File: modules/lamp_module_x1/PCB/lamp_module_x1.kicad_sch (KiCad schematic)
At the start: 24 parts, among them J1 Screw_Terminal_01x02, J2 Screw_Terminal_01x03, J3 Conn_01x06_Socket, J4 Conn_01x03_Socket, K1 12V 5A, Q1 2N7002H, U1 AMS1117-3.3, U2 ESP-12E, U4 PC817

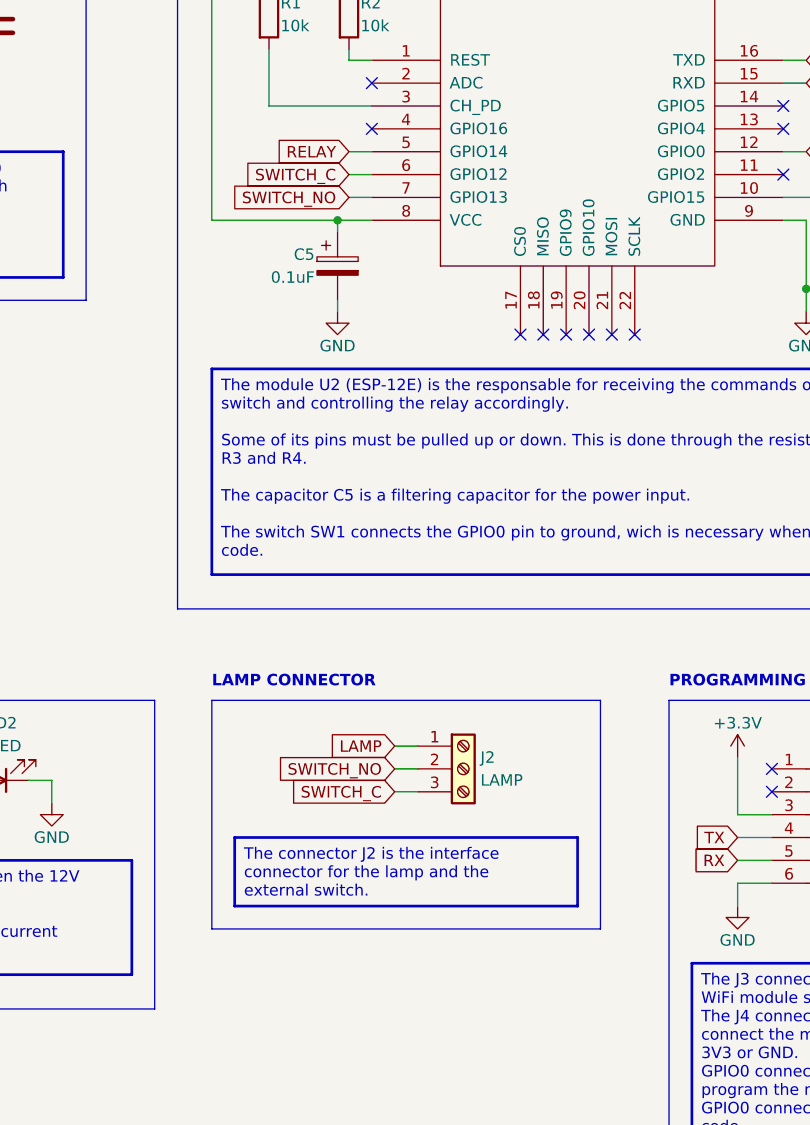
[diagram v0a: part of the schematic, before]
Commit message: Switch feedback implemented
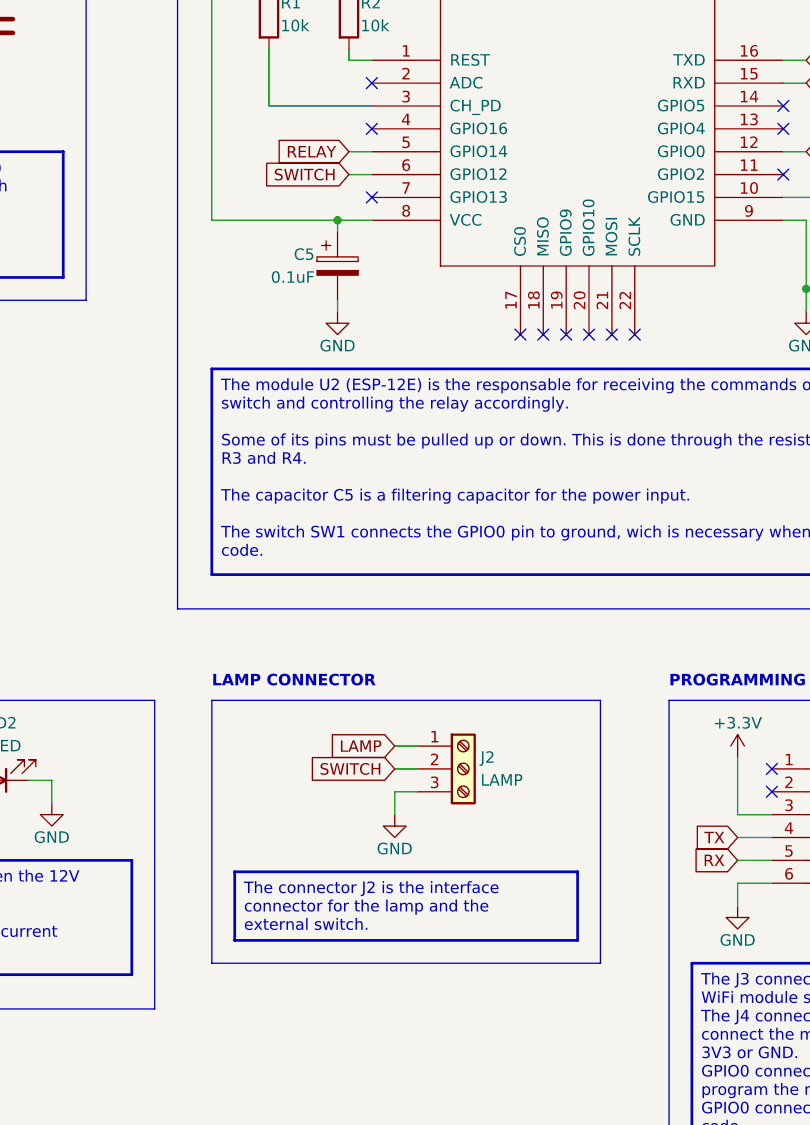
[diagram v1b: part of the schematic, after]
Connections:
- net GND: now also J2.3 (Pin_3)
- net SWITCH_C renamed SWITCH
- net SWITCH: now also J2.2 (Pin_2); no longer J2.3 (Pin_3)
- net SWITCH_NO: no longer names the net of U2.7 (GPIO13)
- net SWITCH_NO: no longer J2.2 (Pin_2)
- no-connect marks 14 -> 15

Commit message: Lamp module X1 PCB finished
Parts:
- removed F1: 0.5A, Fuse:Fuse_0603_1608Metric, symbol Device:Fuse
- added SW1: SW_SPDT, MyLibrary:Toggle_Switch_SelfLocking_7x7, symbol Switch:SW_SPDT
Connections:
- net LINE: now also SW1.2 (B)
- net at J1.2 (Pin_2): now also SW1.3 (C)
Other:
- moved on the sheet: C1, D2, J2, J3, J4, R7

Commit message: Fabrication files updated
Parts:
- renumbered R4 to R3, R5 to R4, R6 to R5, R7 to R6, U4 to U3
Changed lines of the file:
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@@
   (no_connect (at 284.48 123.19))
   (no_connect (at 162.56 144.78))
-  (no_connect (at 257.81 100.33))
   (no_connect (at 303.53 105.41))
   (no_connect (at 303.53 97.79))
+  (no_connect (at 257.81 100.33))
   (no_connect (at 276.86 123.19))
   (no_connect (at 257.81 95.25))
@@
     (stroke (width 0) (type default))
   )
+  (wire (pts (xy 255.27 105.41) (xy 257.81 105.41))
+    (stroke (width 0) (type default))
+  )
   (wire (pts (xy 128.27 90.17) (xy 129.54 90.17))
     (stroke (width 0) (type default))
@@
     (stroke (width 0) (type default))
   )
-  (wire (pts (xy 255.27 105.41) (xy 257.81 105.41))
-    (stroke (width 0) (type default))
-  )
   (wire (pts (xy 104.14 163.83) (xy 106.68 163.83))
     (stroke (width 0) (type default))
@@
     (stroke (width 0) (type default))
   )
+  (wire (pts (xy 255.27 102.87) (xy 257.81 102.87))
+    (stroke (width 0) (type default))
+  )
   (wire (pts (xy 201.93 90.17) (xy 201.93 95.25))
     (stroke (width 0) (type default))
@@
   )
   (wire (pts (xy 134.62 168.91) (xy 135.89 168.91))
-    (stroke (width 0) (type default))
-  )
-  (wire (pts (xy 255.27 102.87) (xy 257.81 102.87))
     (stroke (width 0) (type default))
   )
@@
   (symbol (lib_id "Device:R") (at 134.62 173.99 0) (unit 1)
     (in_bom yes) (on_board yes) (dnp no)
-    (property "Reference" "R6" (at 133.35 172.72 0)
+    (property "Reference" "R5" (at 133.35 172.72 0)
       (effects (font (size 1.27 1.27)) (justify right))
     )
@@
       (project "lamp_module_x1"
         (path "/a46ec17d-39da-44ac-b00f-2365e1778e8f"
-          (reference "R6") (unit 1)
+          (reference "R5") (unit 1)
         )
       )
@@
   (symbol (lib_id "Device:R") (at 311.15 113.03 0) (unit 1)
     (in_bom yes) (on_board yes) (dnp no)
-    (property "Reference" "R4" (at 312.42 111.76 0)
+    (property "Reference" "R3" (at 312.42 111.76 0)
       (effects (font (size 1.27 1.27)) (justify left))
     )
@@
       (project "lamp_module_x1"
         (path "/a46ec17d-39da-44ac-b00f-2365e1778e8f"
-          (reference "R4") (unit 1)
+          (reference "R3") (unit 1)
         )
       )
@@
   (symbol (lib_id "Device:R") (at 110.49 163.83 270) (unit 1)
     (in_bom yes) (on_board yes) (dnp no)
-    (property "Reference" "R5" (at 110.49 158.75 90)
+    (property "Reference" "R4" (at 110.49 158.75 90)
       (effects (font (size 1.27 1.27)))
     )
@@
       (project "lamp_module_x1"
         (path "/a46ec17d-39da-44ac-b00f-2365e1778e8f"
-          (reference "R5") (unit 1)
+          (reference "R4") (unit 1)
         )
       )
@@
   (symbol (lib_id "Device:R") (at 205.74 167.64 270) (unit 1)
     (in_bom yes) (on_board yes) (dnp no)
-    (property "Reference" "R7" (at 205.74 162.56 90)
+    (property "Reference" "R6" (at 205.74 162.56 90)
       (effects (font (size 1.27 1.27)))
     )
@@
       (project "lamp_module_x1"
         (path "/a46ec17d-39da-44ac-b00f-2365e1778e8f"
-          (reference "R7") (unit 1)
+          (reference "R6") (unit 1)
         )
       )
@@
   (symbol (lib_id "Isolator:PC817") (at 123.19 166.37 0) (unit 1)
     (in_bom yes) (on_board yes) (dnp no)
-    (property "Reference" "U4" (at 123.19 158.75 0)
+    (property "Reference" "U3" (at 123.19 158.75 0)
       (effects (font (size 1.27 1.27)))
     )
@@
       (project "lamp_module_x1"
         (path "/a46ec17d-39da-44ac-b00f-2365e1778e8f"
-          (reference "U4") (unit 1)
-        )
-      )
+          (reference "U3") (unit 1)
+        )
+      )
